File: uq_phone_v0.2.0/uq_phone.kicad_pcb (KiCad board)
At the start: 6 copper layers, 45 x 108 mm, 200 parts, among them J1 PJ-605-6A, J2 124018312112A, J3 BM03B-ACHSS-GAN-TF_LF__SN_, J6 Conn_ARM_SWD_TagConnect_TC2030, J7 559092474, J8 MCS-302S-C1, J9 559092474, M1 C08-00A, Q1 MMBT3904LP-7, Q2 MMBT3904LP-7, Q3 S8050, Q4 DMP2035U-7, Q5 MMBT3904LP-7, Q6 MMBT3904LP-7, SW1 SKTAAAE010, SW10 SKTAAAE010, SW11 SKTAAAE010, SW12 SKTAAAE010, SW13 SKTAAAE010, SW14 SKTAAAE010, SW15 SKTAAAE010, SW16 SKSCLCE010, SW17 SKTAAAE010, SW18 SKTAAAE010, SW19 SKTAAAE010, SW2 SKTAAAE010, SW20 SKTAAAE010, SW21 SKTAAAE010, SW22 SKSCLCE010, SW23 SKTAAAE010, SW24 SKTAAAE010, SW25 SKTAAAE010, SW26 SKTAAAE010, SW27 SKTAAAE010, SW28 SKTAAAE010, SW29 SKTAAAE010, SW3 SKTAAAE010, SW30 SKTAAAE010, SW31 SKTAAAE010, SW32 SKTAAAE010, SW33 SKTAAAE010, SW34 SKTAAAE010, SW35 SKTAAAE010, SW36 SKTAAAE010, SW37 SKTAAAE010, SW38 SKTAAAE010, SW39 SKTAAAE010, SW4 SKTAAAE010, SW40 SKTAAAE010, SW41 SKTAAAE010, SW5 SKTAAAE010, SW6 SKSCLCE010, SW7 SKTAAAE010, SW8 SKTAAAE010, SW9 SKTAAAE010, U1 TPS62162DSGR, U10 TPD8F003DQDR, U11 LSM6DSVTR, U12 DRV2603RUNR, U13 TS3A5018RSVR, U14 NAU88C22YG, U15 TPS22964CYZPR, U17 TXU0204DTRR, U18 TXU0304DTRR, U19 TXU0104DTRR, U2 MCP73871-2CCI_ML, U20 TXU0104DTRR, U3 BQ27441DRZR-G1A, U5 TCA9509MRVHR, U6 STM32H723VGHx, U7 TPS22964CYZPR, U8 TPD3F303DQDR, U9 AZV5001RA4-7

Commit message: Update SD card power routing
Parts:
- moved U7 9.45 mm to (52.0, 50.4), turned to 0 degrees
- moved Q6 9.12 mm to (57.8, 43.3), turned to 90 degrees
- moved R37 3.30 mm to (51.9, 45.5), turned to 180 degrees
- moved C22 2.94 mm to (51.8, 48.8), turned to 180 degrees
- moved C23 1.88 mm to (51.8, 47.8), turned to 0 degrees
- moved R29 1.40 mm to (51.9, 46.3), turned to 180 degrees
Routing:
- net SD_PWR_EN: track 0.00 -> 34.3 mm, vias 0 -> 5
- net SD_VDD_SW: track 0.00 -> 32.1 mm, vias 0 -> 5
- net uSD_TRAY_DET: track 4.87 -> 32.5 mm, vias 3 -> 4
- net +3.3V: track 239.7 -> 264.8 mm, vias 26 -> 27
- net Net-(Q6-Pad1): track 0.00 -> 6.35 mm, vias 0 -> 2
- net GND: track 86.5 -> 88.6 mm
- net HP_DET: track 86.4 -> 85.4 mm
- net PWR_BUTTON_SENSE: track 35.2 -> 35.7 mm

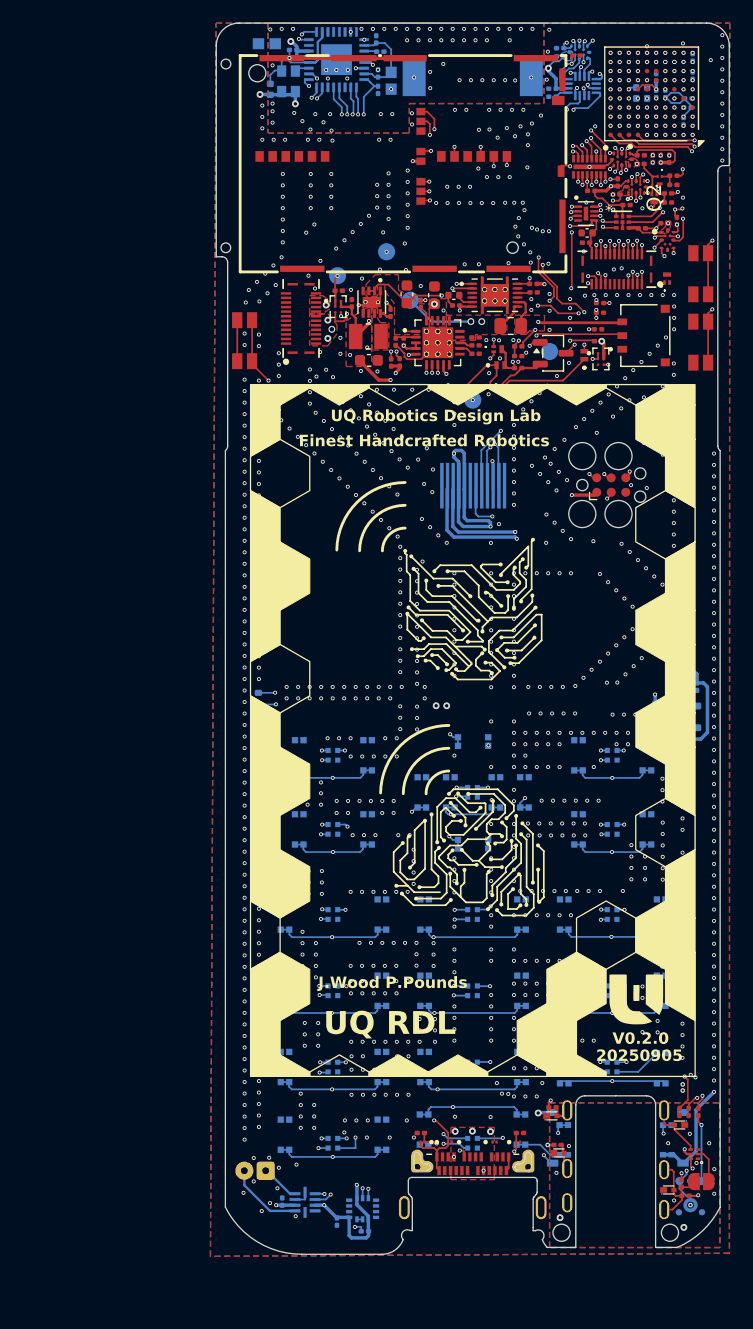
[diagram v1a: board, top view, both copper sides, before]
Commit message: Add headphone breakout board and update main PCB
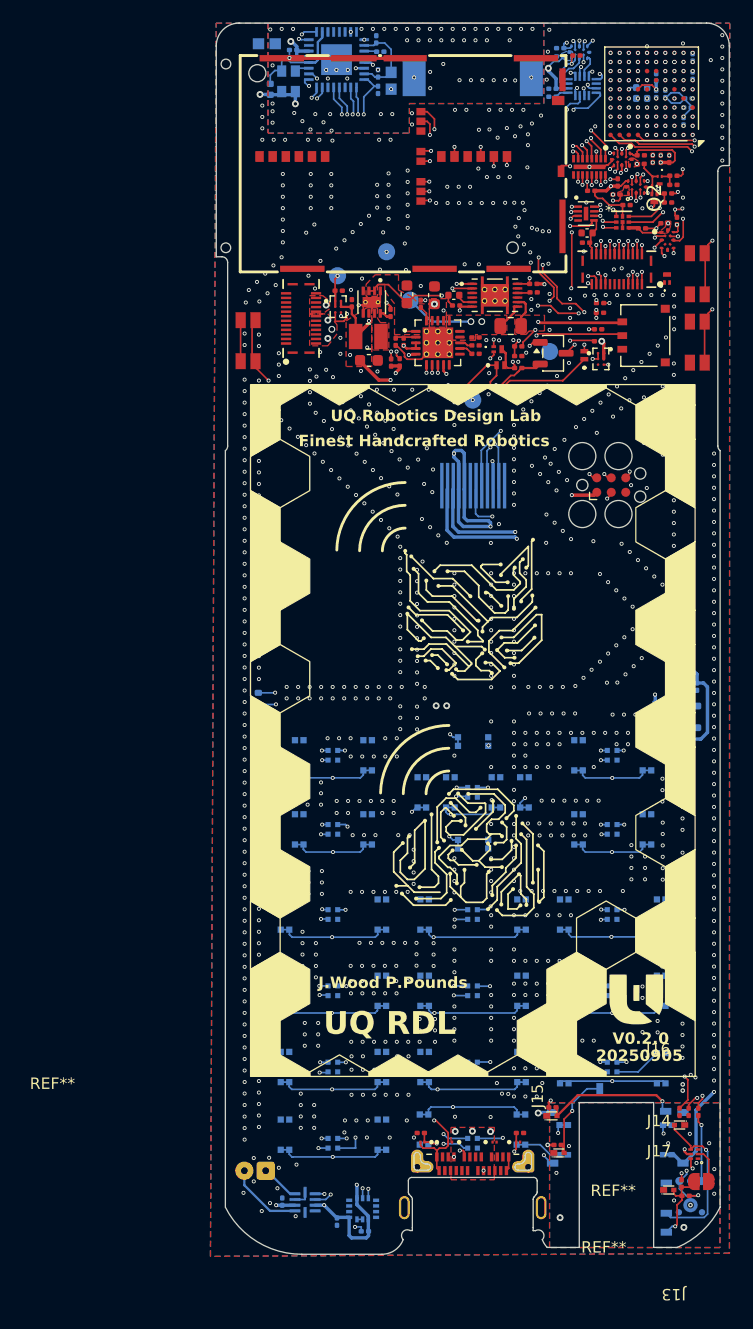
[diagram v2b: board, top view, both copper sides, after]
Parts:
- removed ? (x2): , 
- removed J1: PJ-605-6A, custom_footprints:AUDIO-TH_PJ-605-6A
- added J13: Conn_01x01, headphone_board:Breakout_Mating_Pad, F.Cu at (58.5, 127.5)
- added J14: Conn_01x01, headphone_board:Breakout_Mating_Pad, F.Cu at (56.9, 122.1)
- added J15: Conn_01x01, headphone_board:Breakout_Mating_Pad, F.Cu at (51.4, 115.2)
- added J16: Conn_01x01, headphone_board:Breakout_Mating_Pad, F.Cu at (56.9, 115.8)
- added J17: Conn_01x01, headphone_board:Breakout_Mating_Pad, F.Cu at (56.9, 124.7)
- added REF**: Breakout 3D, headphone_board:breakout 3d, F.Cu at (3.89, 114.4)
- added REF**: Headphone_Breakout_3D, headphone_board:Untitled_2, F.Cu at (53.1, 123.8)
- added REF**: Breakout 3D, headphone_board:breakout 3d, F.Cu at (52.3, 128.8)
- moved SW16 0.30 mm to (60.5, 48.9)
- moved SW6 0.30 mm to (60.5, 42.9)
- moved SW22 0.30 mm to (21.1, 48.8)
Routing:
- net Net-(J16-Pin_1): track 2.03 -> 12.0 mm, vias 0 -> 1
- net HP_LEFT_DET: track 4.83 -> 13.9 mm, vias 0 -> 1
- net Net-(J15-Pin_1): track 2.36 -> 8.39 mm, vias 0 -> 1
- net SD_VDD_SW: track 32.1 -> 30.8 mm
- net MIC_PIN: track 8.28 -> 7.40 mm, vias 0 -> 1
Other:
- outline, holes or cut-outs redrawn

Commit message: Updated main PCB
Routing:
- net AGND: track 0.00 -> 1.56 mm, vias 69 -> 71
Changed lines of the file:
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@@
 		(net 10)
 	)
+	(segment
+		(start 47.25 116.93)
+		(end 47.77 117.45)
+		(width 0.3)
+		(layer "F.Cu")
+		(net 11)
+	)
+	(segment
+		(start 60.83 119.7)
+		(end 61.07 119.94)
+		(width 0.15)
+		(layer "F.Cu")
+		(net 11)
+	)
+	(segment
+		(start 47.25 116.75)
+		(end 47.25 116.93)
+		(width 0.3)
+		(layer "F.Cu")
+		(net 11)
+	)
+	(segment
+		(start 60.525 119.7)
+		(end 60.83 119.7)
+		(width 0.15)
+		(layer "F.Cu")
+		(net 11)
+	)
 	(via
 		(at 38 21.4)
@@
 	)
 	(via
+		(at 47.77 117.45)
+		(size 0.35)
+		(drill 0.2)
+		(layers "F.Cu" "B.Cu")
+		(free yes)
+		(net 11)
+	)
+	(via
 		(at 37 21.4)
 		(size 0.35)
@@
 	)
 	(via
+		(at 61.1 119.96)
+		(size 0.35)
+		(drill 0.2)
+		(layers "F.Cu" "B.Cu")
+		(free yes)
+		(net 11)
+	)
+	(via
 		(at 44 21.4)
 		(size 0.35)
@@
 	)
 	(segment
-		(start 60.911 119.414)
-		(end 61.222484 119.725484)
+		(start 58.45 117.95)
+		(end 58.45 117.55)
 		(width 0.15)
 		(layer "F.Cu")
@@
 	(segment
 		(start 58.45 117.95)
-		(end 58.45 117.55)
+		(end 59.875 119.375)
 		(width 0.15)
 		(layer "F.Cu")
@@
 	)
 	(segment
-		(start 59.875 119.7)
-		(end 60.161 119.414)
+		(start 61.03 119.31)
+		(end 61.36 119.64)
 		(width 0.15)
 		(layer "F.Cu")
@@
 	)
 	(segment
-		(start 58.45 117.95)
-		(end 59.875 119.375)
+		(start 61.36 119.64)
+		(end 61.367941 119.647941)
 		(width 0.15)
 		(layer "F.Cu")
@@
 	)
 	(segment
-		(start 60.161 119.414)
-		(end 60.911 119.414)
+		(start 59.875 119.375)
+		(end 59.875 119.7)
 		(width 0.15)
 		(layer "F.Cu")
@@
 	)
 	(segment
-		(start 59.875 119.375)
-		(end 59.875 119.7)
+		(start 59.875 119.7)
+		(end 60.265 119.31)
+		(width 0.15)
+		(layer "F.Cu")
+		(net 205)
+	)
+	(segment
+		(start 60.265 119.31)
+		(end 61.03 119.31)
+		(width 0.15)
+		(layer "F.Cu")
+		(net 205)
+	)
+	(segment
+		(start 61.367941 119.647941)
+		(end 61.367941 119.649523)
 		(width 0.15)
 		(layer "F.Cu")
@@
 	)
 	(via
-		(at 61.222484 119.725484)
+		(at 61.36 119.64)
 		(size 0.35)
 		(drill 0.2)
@@
 	)
 	(segment
-		(start 61.058613 125.662346)
-		(end 58.112346 125.662346)
+		(start 61.49 125.230959)
+		(end 61.058613 125.662346)
 		(width 0.15)
 		(layer "B.Cu")
@@
 	)
 	(segment
-		(start 61.222484 119.725484)
-		(end 61.36 119.863)
+		(start 61.49 119.77)
+		(end 61.49 125.230959)
 		(width 0.15)
 		(layer "B.Cu")
@@
 	)
 	(segment
-		(start 61.36 125.360959)
-		(end 61.058613 125.662346)
+		(start 58.112346 125.662346)
+		(end 57.74 125.29)
 		(width 0.15)
 		(layer "B.Cu")
@@
 	)
 	(segment
-		(start 61.36 119.863)
-		(end 61.36 125.360959)
+		(start 61.36 119.64)
+		(end 61.49 119.77)
 		(width 0.15)
 		(layer "B.Cu")
@@
 	)
 	(segment
-		(start 58.112346 125.662346)
-		(end 57.74 125.29)
+		(start 61.058613 125.662346)
+		(end 58.112346 125.662346)
 		(width 0.15)
 		(layer "B.Cu")
@@
 	)
 	(segment
-		(start 60.525 120.1)
-		(end 61 120.1)
+		(start 61.21 120.55)
+		(end 61.465 120.805)
 		(width 0.15)
 		(layer "F.Cu")
@@
 	)
 	(segment
-		(start 61 120.1)
-		(end 61.465 120.565)
+		(start 61.465 120.805)
+		(end 61.465 122.51)
 		(width 0.15)
 		(layer "F.Cu")
@@
 	)
 	(segment
-		(start 61.465 120.565)
-		(end 61.465 122.51)
+		(start 60.525 120.1)
+		(end 60.76 120.1)
+		(width 0.15)
+		(layer "F.Cu")
+		(net 206)
+	)
+	(segment
+		(start 60.76 120.1)
+		(end 61.21 120.55)
 		(width 0.15)
 		(layer "F.Cu")
